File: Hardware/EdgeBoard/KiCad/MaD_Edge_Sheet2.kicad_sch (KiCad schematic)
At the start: 101 parts, among them IC1 ISO6742DWR, IC10 NSI50010YT1G, IC11 NSI50010YT1G, IC12 NSI50010YT1G, IC13 NSI50010YT1G, IC2 ISO6742DWR, IC3 UCC12040DVER, IC4 UCC12040DVER, IC5 ISO6731DWR, IC6 NSI50010YT1G, IC7 NSI50010YT1G, IC8 NSI50010YT1G, IC9 NSI50010YT1G, J10 ChargePump, J11 ESDUpper, J12 ESDLower, J13 ESDActive, J14 ENDUpper, J15 ENDLower, J16 Door, J17 GPI_3, J18 GPI_4, J19 NavKey, J4 436500321, J5 GPO_2, J6 GPO_1, J7 GPI_2, J8 GPI_1, J9 Force, U10 SN74LVC1G14DBV, U11 SN74LVC1G14DBV, U12 SN74LVC1G14DBV, U13 SN74LVC1G14DBV, U14 SN74LVC1G14DBV, U15 SN74LVC1G14DBV, U16 SN74LVC1G14DBV, U17 SN74LVC1G14DBV, U18 SN74LVC1G14DBV, U19 SN74LVC1G14DBV, U21 SN74LVC1G14DBV, U22 SN74LVC1G14DBV, U4 6N137, U5 VO2631, U6 VO2631, U7 VO2631, U8 VO2631, U9 SN74LVC1G14DBV

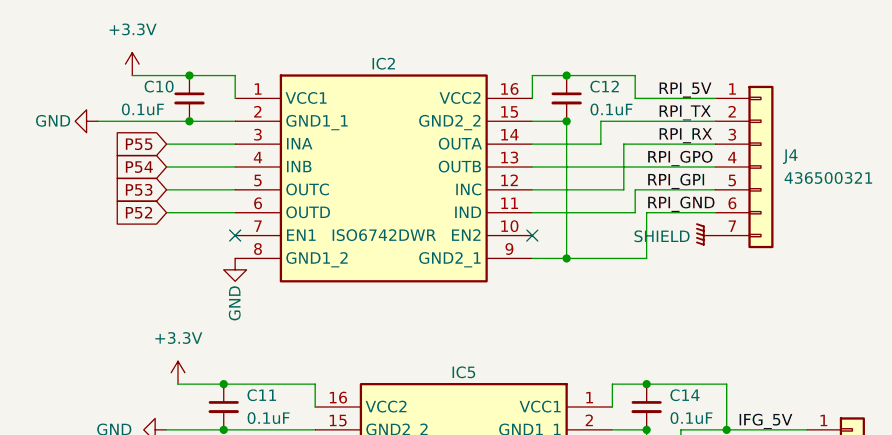
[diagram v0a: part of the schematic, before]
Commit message: Edge carrier revision: fixes from the SIL hardware findings (#309)
* fix(hardware): servo enable off at power-up: IC14 ISO7741FDWR and a P6 pull-down

Finding SRV-F6. Nothing pulls P6 (servo enable request), and the fitted
non-F IC14 outputs high from an open or unpowered input, so the drive
enable is on through reset, boot and flashing.

- IC14 becomes ISO7741FDWR (LCSC C485810): same pinout (TI SLLSEP4K
  Table 4-1 p.5); with the F suffix an open input or an unpowered side 1
  gives a low output (Table 7-2 p.29). Value, MPN, LCSC and notes updated.
- R39, 10 k (0603WAF1002T5E, C25804) from P6 to GND. On the PCB it sits
  by IC14 and joins the P6 trace at U29 through two 0.6 mm vias and B.Cu.
- STEP/DIR (P8/P7) now also rest low when undriven.

Co-Authored-By: Claude Opus 5.5 <noreply@anthropic.com>

* fix(hardware): Q1 drawn and laid out as the fitted SOT-23 MMBT3904

Finding SRV-F8-Q1. Q1 used the TO-92 2N3904 symbol (1 E, 2 B, 3 C) but
the part fitted is a SOT-23 MMBT3904 (1 B, 2 E, 3 C; JSCJ datasheet,
LCSC C20526, p.1), so JP1's open-collector position could never enable
the drive.

- Symbol Transistor_BJT:MMBT3904, footprint Package_TO_SOT_SMD:SOT-23.
- PCB: Q1 rotated -90 so base faces R24; base to R24, emitter to a new
  EN_GND via, collector to JP1 pin 3. The old emitter trace and via go.

Co-Authored-By: Claude Opus 5.5 <noreply@anthropic.com>

* fix(hardware): U25 AM26C32IDR (5 V receiver) with its own 0.1 uF

Finding ENC-F3. U25 (AM26LV32IDR, 3.0-3.6 V, TI SLLS202H 6.3) runs from
the 5 V SC_5V rail.

- U25 becomes AM26C32IDR (LCSC C36693): pin-identical (TI SLLS104M
  Table 4-1 p.3), VCC 4.5-5.5 V (5.3 p.4), VOH >= 3.8 V at -6 mA (5.6
  p.5), above IC16's 0.7 x VCC1 input threshold. KiCad has no AM26C32
  symbol; the AM26LV32xD symbol stays.
- C30, 0.1 uF 0402 (CL05B104KO5NNNC, C1525) from U25.16 to EN_GND,
  beside the pin. 0402 is the size that fits between JP2 and U25.

Co-Authored-By: Claude Opus 5.5 <noreply@anthropic.com>

* fix(hardware): U25 alw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
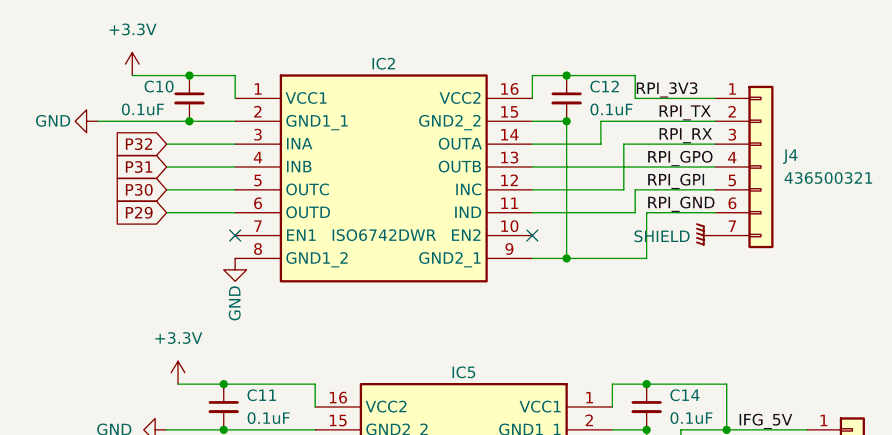
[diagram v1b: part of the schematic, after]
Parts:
- C10, C11, C12, C13, C14, C15, C18, C19, C20, C21, C22, C23, C7, C8, C9: DIGIKEY 1276-1043-1-ND -> (none); MANUFACTURER Samsung Electro-Mechanics -> YAGEO; Manufacturer_Part_Number CL05A104KA5NNNC -> CC0603KRX7R9BB104
- IC1: LCSC C2862403 -> C5216407; NOTES Pin Compatible with ISO77xx -> Pin compatible with ISO77xx. Ordered as the non-F ISO6742DW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; manufacturer_part_number_1 ISO6742DWR or ISO7742FDWR -> ISO6742DWR
- IC2: LCSC C2862403 -> C5216407; NOTES Pin Compatible with ISO77xx -> Non-F (default-high) part only: UART lines idle high. VCC2 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; manufacturer_part_number_1 ISO6742DWR or ISO7742FDWR -> ISO6742DWR
- J4: footprint Connector_Molex:Molex_Micro-Fit_3.0_43045-0615_2x03_P3.00mm_Vertical -> Connector_Molex:Molex_Micro-Fit_3.0_43045-0618_2x03-1MP_P3.00mm_Vertical
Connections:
- net P52 renamed P29
- net P53 renamed P30
- net P54 renamed P31
- net P55 renamed P32
- net RPI_5V renamed RPI_3V3
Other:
- company: (none) -> MaD
- title: (none) -> MaD Edge carrier: I/O and host link
